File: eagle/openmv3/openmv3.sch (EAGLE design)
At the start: 56 parts, among them Q1 MOSFET, U1 STM32F765VGT6, U2 OV7725, U3 BD33IA, X1 47571-0001, X2 MICROUSB-RIGHT, Y1 7S-12.000MAHE-T

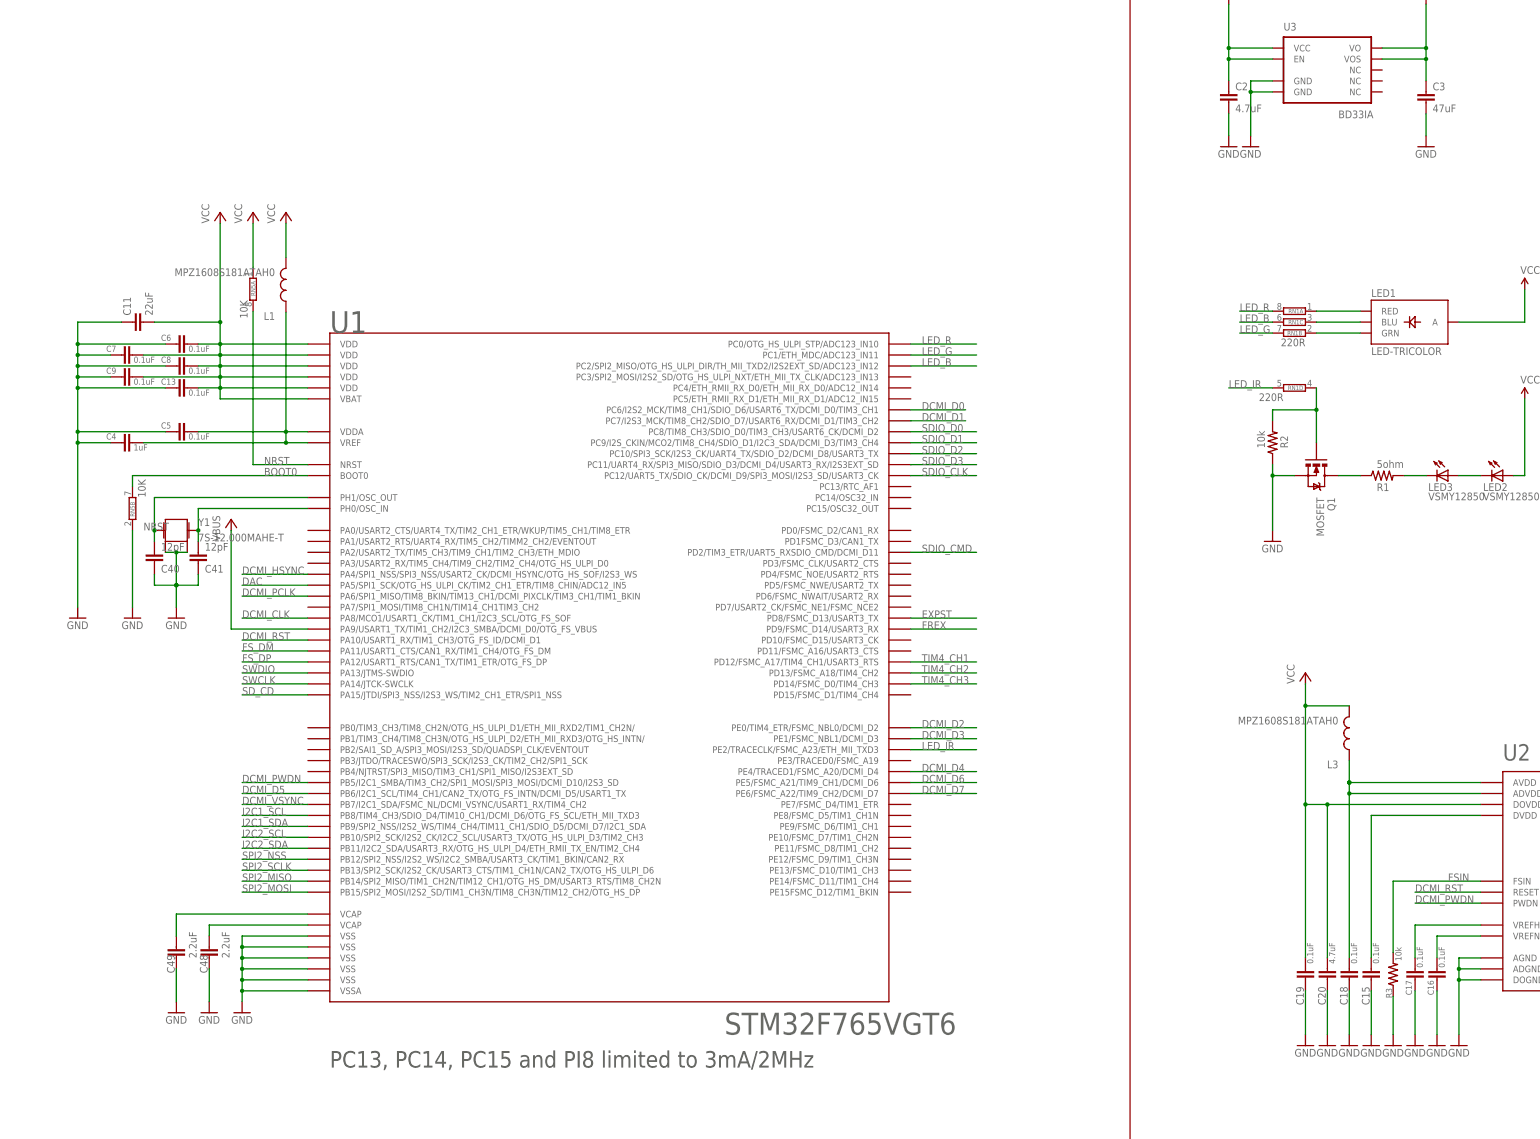
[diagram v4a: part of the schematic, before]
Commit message: Update OMV3 Eagle files.
* Add 22uF for the uSD
* Add 22uf for reg input
* Add 47uF near the MCU
* Add 47uF near the sensor
* Add 22uF for sensor digital input
* Replace sensor bead with RC filter on AVDD
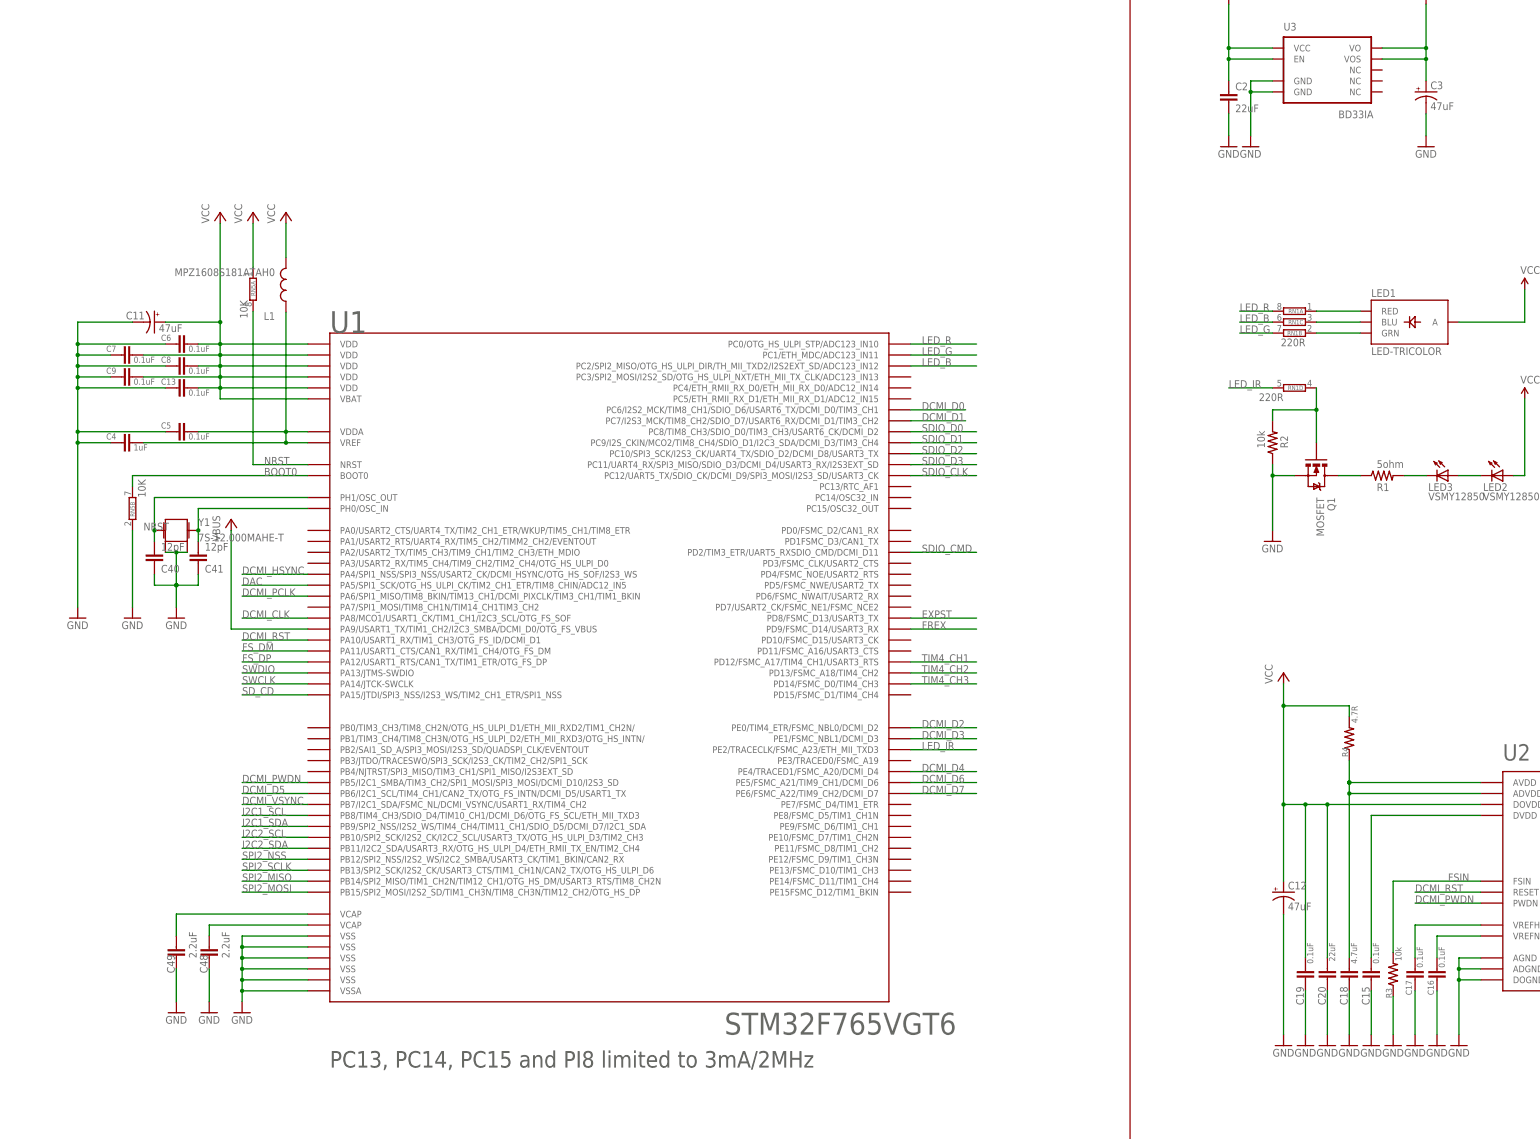
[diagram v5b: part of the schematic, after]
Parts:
- removed L3: MPZ1608S181ATAH0, sfe:INDUCTOR0603
- added C12: 47uF, sfe:CAP_POL1206
- added R4: 4.7R, sfe:RESISTOR0603-RES
- C11: value 22uF -> 47uF; device sfe:CAP0805 -> sfe:CAP_POL1206
- C18: value 0.1uF -> 4.7uF
- C2, C20: value 4.7uF -> 22uF; device sfe:CAP0603-CAP -> sfe:CAP0805
- C3: device sfe:CAP1206 -> sfe:CAP_POL1206
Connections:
- net GND: now also C11.-, C12.-, C3.-; no longer C11.1, C3.2
- net N$13: now also R4.1; no longer L3.1
- net VCC: now also C11.+, C12.+, C3.+, R4.2; no longer C11.2, C3.1, L3.2

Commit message: Update OMV3 Eagle Files.
* Fix some parts names.
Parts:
- R1: value 5ohm -> 10R
- RN4: value 10K -> 4.7K
- X2: value MICROUSB-RIGHT -> MF-CON-MICROUSB-RIGHT
- renumbered RN5 to RN2, RN6 to RN3, RN7 to RN4

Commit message: Cleanup OpenMV-3 schematics.
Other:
- note added: "DEBUG HEADER"
- note added: "I/O HEADERS"
- note added: "IMAGE SENSOR"
- note added: "IR-RGB LEDs"
- note added: "No external termination series resistors are required on DP (D+) and DM (D-) pins since the matching impedance is included in the embedded driver."
- note added: "Notes:"
- note added: "SD CARD"
- note added: "STM32F7xx MCU"
- note added: "USB & POWER SUPPLY"
- moved on the sheet: C1, C10, C11, C12, C13, C15, C16, C17, C18, C19, C2, C20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
